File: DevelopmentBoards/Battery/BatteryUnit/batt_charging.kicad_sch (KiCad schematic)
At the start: 2 parts, among them U2 BQ25713RSNR

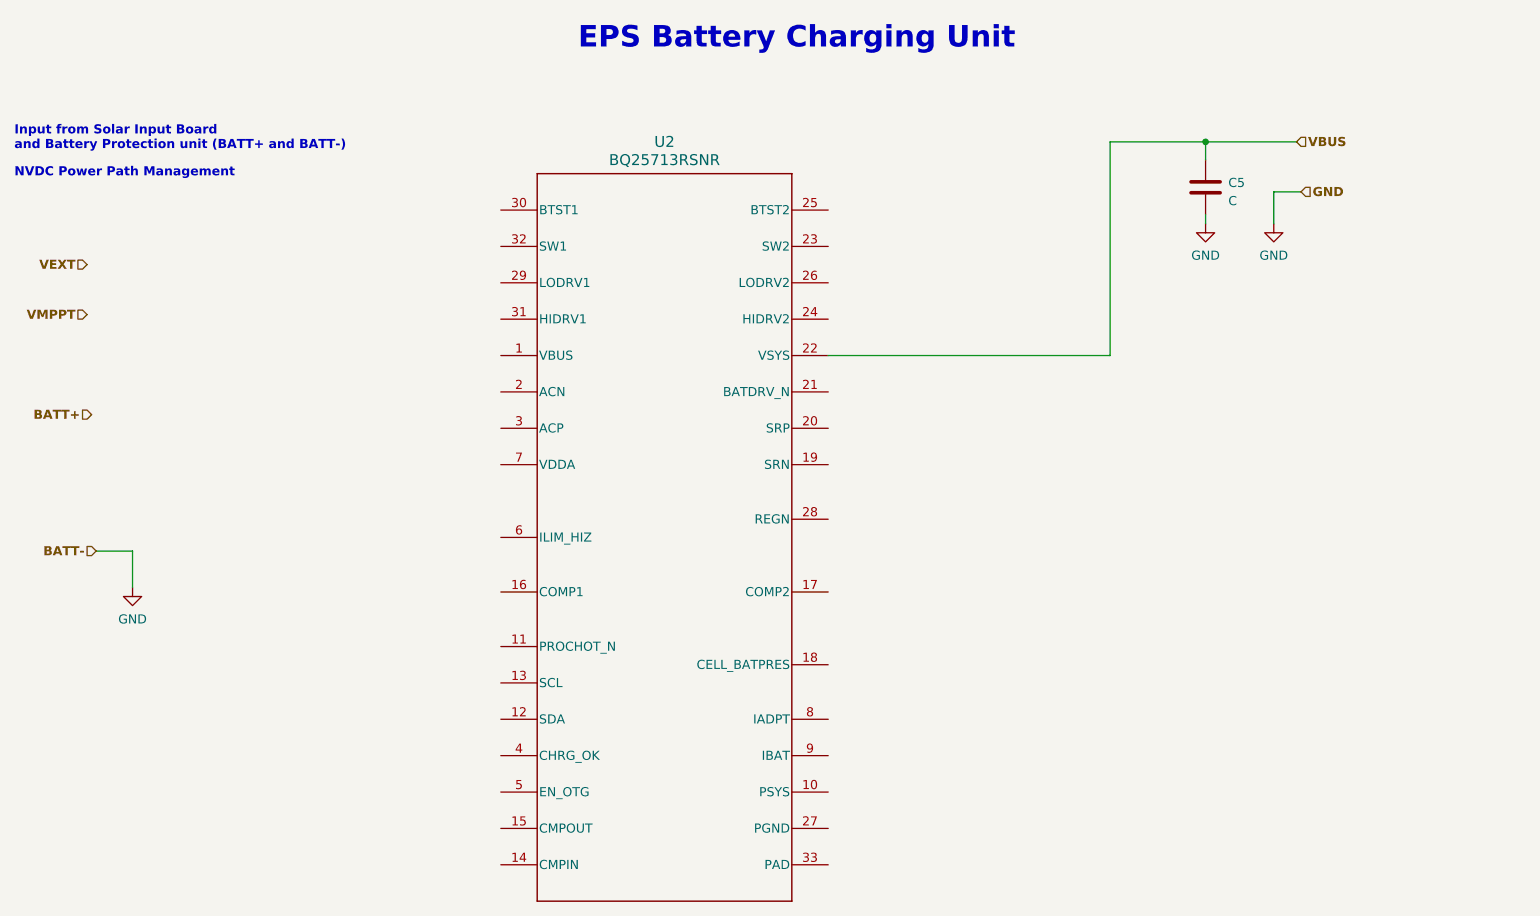
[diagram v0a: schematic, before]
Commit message: EPS Final Board
Started EPS final board schematic
yet to add dependencies of external libraries to a common folder on GitHub
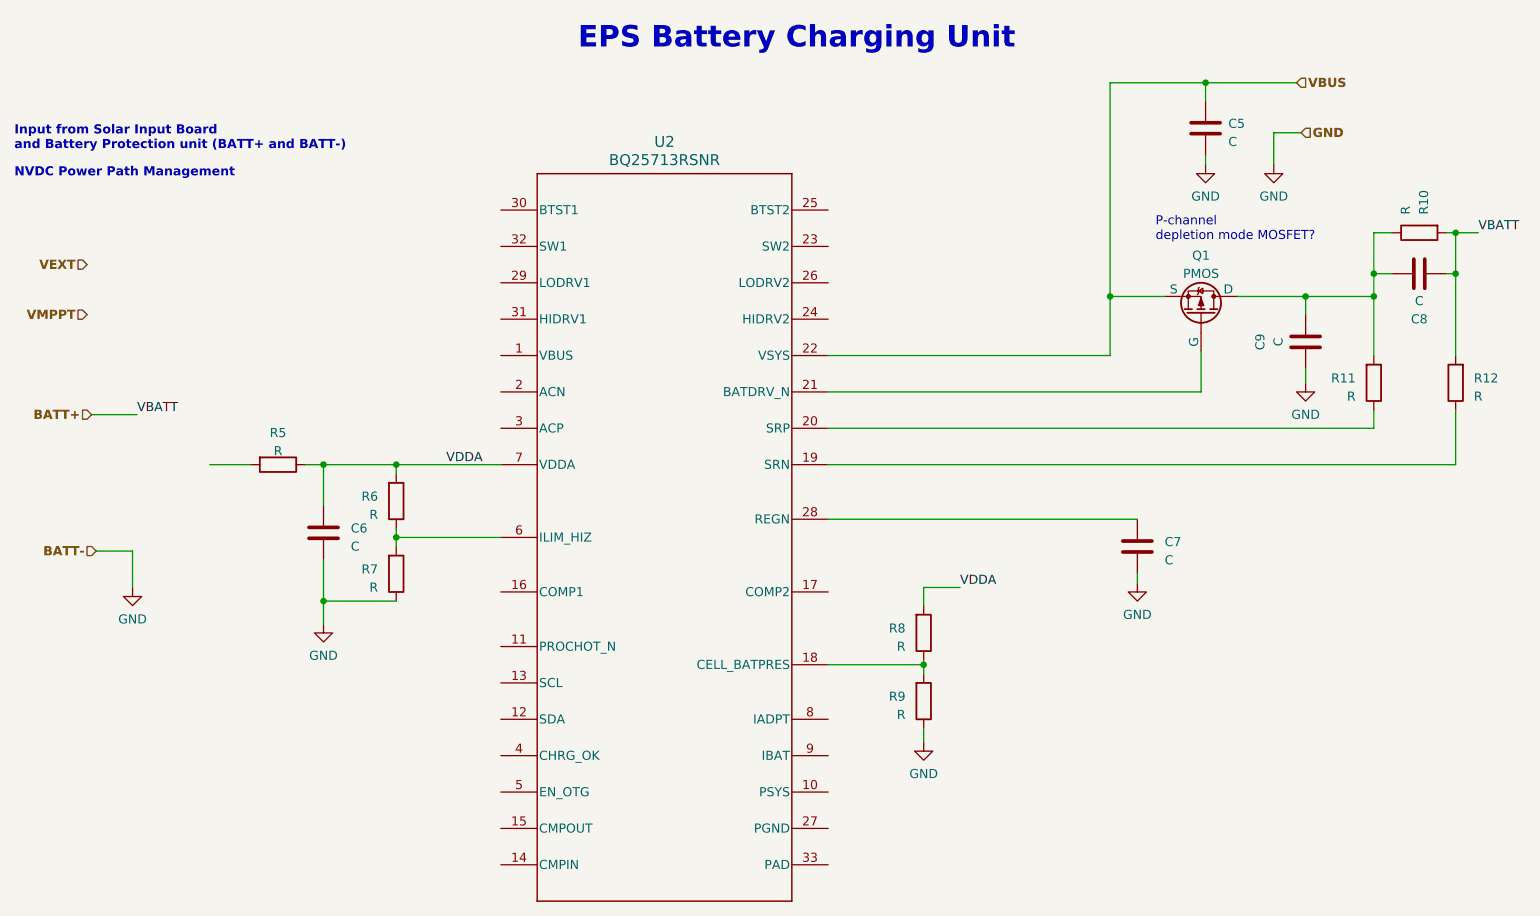
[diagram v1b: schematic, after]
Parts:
- added C6, C7, C8, C9: C, symbol Device:C
- added Q1: PMOS, symbol Simulation_SPICE:PMOS
- added R10, R11, R12, R5, R6, R7, R8, R9: R, symbol Device:R
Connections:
- net BATT+: now also C8.1, R10.2, R12.2
- net GND: now also C6.2, C7.2, C9.1, R7.1, R9.1
- net VBUS: now also Q1.3 (S)
- net at U2.18 (CELL_BATPRES): now also R8.1, R9.2
- net at U2.19 (SRN): now also R12.1
- net at U2.20 (SRP): now also R11.1
- net at U2.21 (BATDRV_N): now also Q1.2 (G)
- net at U2.28 (REGN): now also C7.1
- net at U2.6 (ILIM_HIZ): now also R6.1, R7.2
- net VDDA: now reaches U2.7 (VDDA)
- net VDDA: now also C6.1, R5.1, R6.2, R8.2
- new net: C8.2, C9.2, Q1.1 (D), R10.1, R11.2
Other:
- note added: "P-channel depletion mode MOSFET?"
- moved on the sheet: C5
